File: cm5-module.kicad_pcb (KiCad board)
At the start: 4 copper layers, 100 x 100 mm, 205 parts, among them J1 DIN-41612-connector_090319679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, J10 MicroSD_5033981892, J11 JST_SH_1x4_BM04B-SRSS-TB-LF-SN, J2 CM5_1-100_3mm-stack, J3 CM5_101-200_3mm-stack, J4 JST_SH_1x3_BM03B-SRSS-TB-LF-SN, J5 Bus_M.2_1-2199230-6, J6 RJ45_HC612601A-M893-A, J7 USB-A_USB-303WSD-BRY, J8 HDMI-A_HDMI-19PIN-043, J9 USB-C_USB-310F-B-SU, Q1 SIS472DN-T1-GE3, Q2 SIS472DN-T1-GE3, Q3 AO3400A, Q4 SIS472DN-T1-GE3, SW1 SW_TL2243, U1 AP22615AWU-7, U10 AP22615AWU-7, U11 AP22615AWU-7, U12 LM74700QDBVRQ1, U13 STM32G431CBU6, U14 STM32G431CBU6, U15 TJA1044GTK_3Z, U16 TJA1044GTK_3Z, U2 AP22615AWU-7, U3 FT230XQ-R, U4 NTS0102DP, U5 CH334P, U6 LM74700QDBVRQ1, U7 SIC431AED-T1-GE3, U8 LM74700QDBVRQ1, U9 TPS564247DRLR, Y1 Oscillator_32.768kHz_OK2EL89C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, Y2 X322512MSB4SI

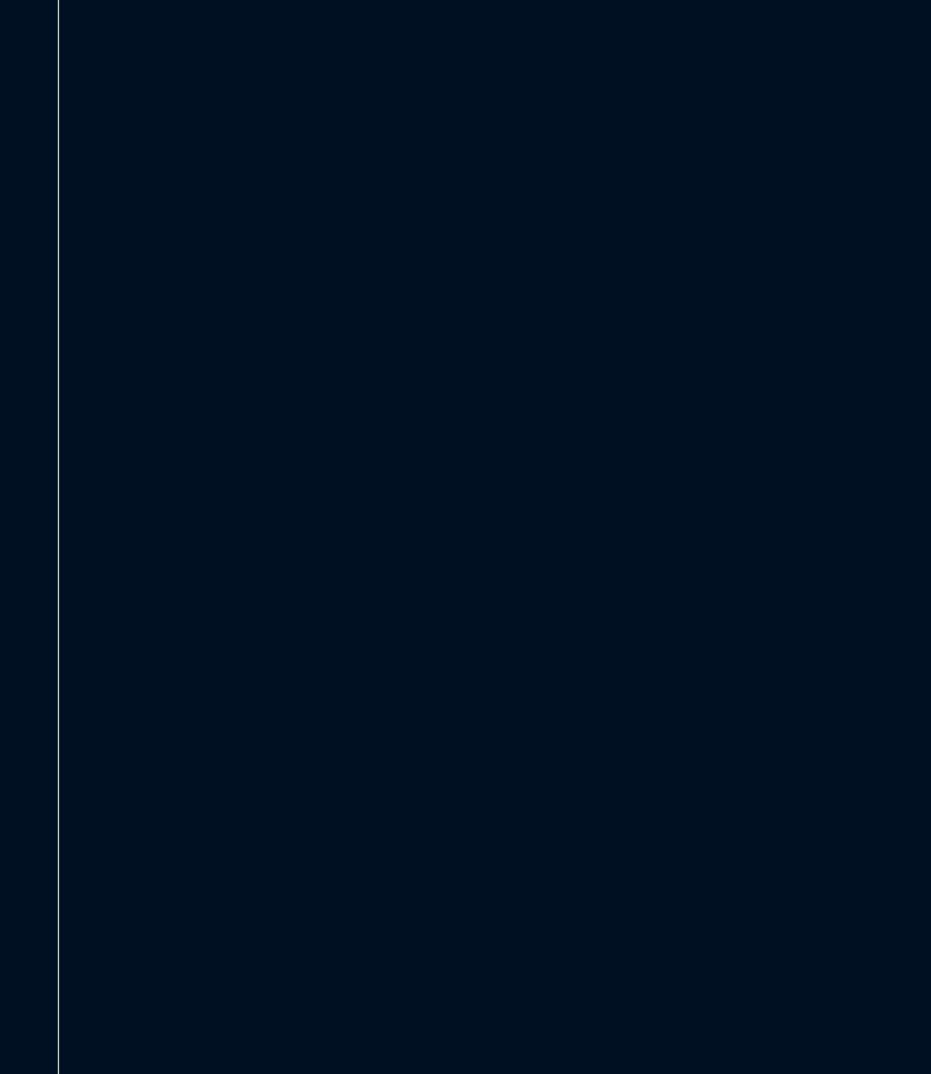
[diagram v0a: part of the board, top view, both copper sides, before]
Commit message: [#1] Add USB switch and 0R to USB hub data lines, minor schematic refactor
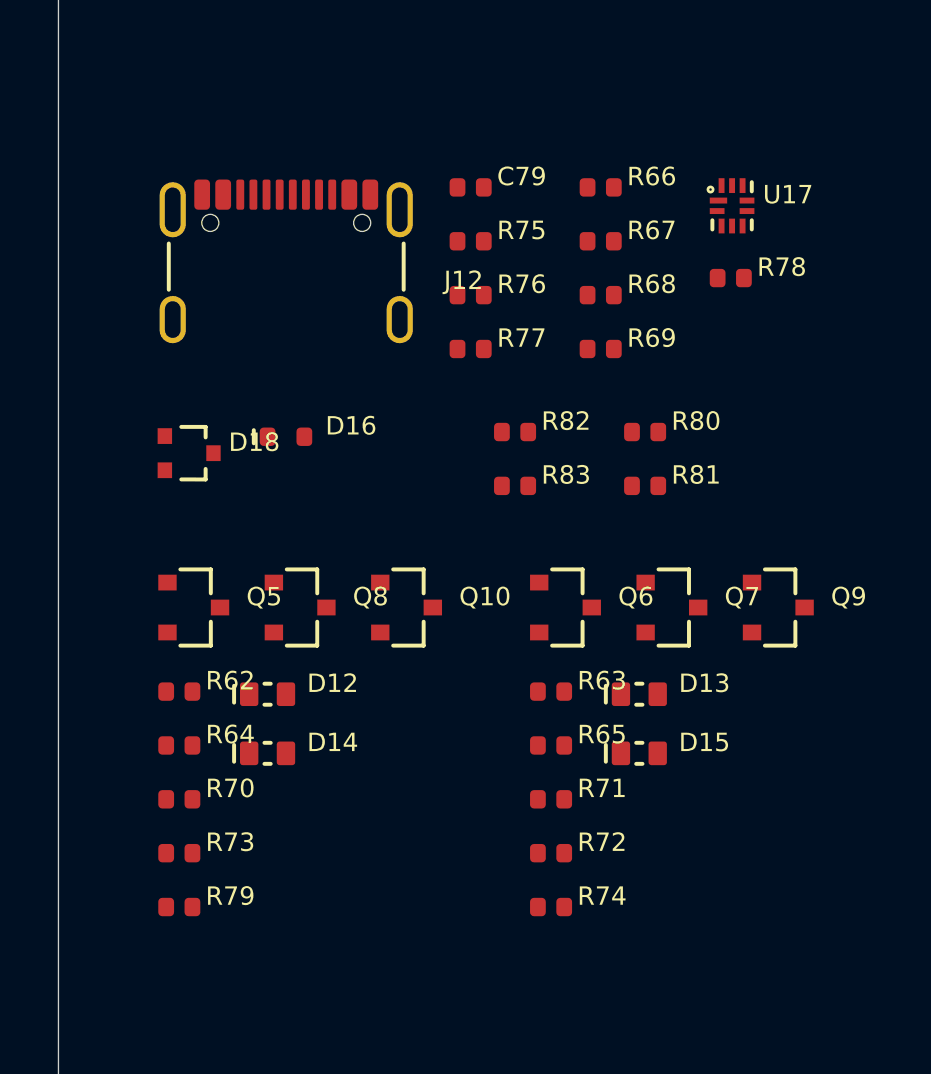
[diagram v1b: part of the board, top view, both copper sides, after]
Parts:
- added C79: C-100n-0402, DW-footprints:C_0402_1005Metric, F.Cu at (155.1, 67.2)
- added D12: LED-R-0603_KT-0603R, DW-footprints:LED_0603_1608Metric_R, F.Cu at (147.3, 86.5)
- added D13: LED-R-0603_KT-0603R, DW-footprints:LED_0603_1608Metric_R, F.Cu at (161.5, 86.5)
- added D14: LED-R-0603_KT-0603R, DW-footprints:LED_0603_1608Metric_R, F.Cu at (147.3, 88.8)
- added D15: LED-R-0603_KT-0603R, DW-footprints:LED_0603_1608Metric_R, F.Cu at (161.5, 88.8)
- added D16: PESD5Z5, DW-footprints:D_SOD-523, F.Cu at (148.0, 76.7)
- added D18: TPD2E2U06DCKR, DW-footprints:SOT-323, F.Cu at (144.3, 77.3)
- added J12: USB-C_USB-310F-B-SU, DW-footprints:USB-C-Receptacle_USB-310-B-SU, F.Cu at (148.0, 71.2)
- added Q10: AO3400A, DW-footprints:SOT-23-3, F.Cu at (152.6, 83.2)
- added Q5: AO3400A, DW-footprints:SOT-23-3, F.Cu at (144.5, 83.2)
- added Q6: AO3400A, DW-footprints:SOT-23-3, F.Cu at (158.7, 83.2)
- added Q7: AO3400A, DW-footprints:SOT-23-3, F.Cu at (162.7, 83.2)
- added Q8: AO3401A, DW-footprints:SOT-23-3, F.Cu at (148.6, 83.2)
- added Q9: AO3401A, DW-footprints:SOT-23-3, F.Cu at (166.8, 83.2)
- added R62: R-1k-0402, DW-footprints:R_0402_1005Metric, F.Cu at (144.0, 86.4)
- added R63: R-1k-0402, DW-footprints:R_0402_1005Metric, F.Cu at (158.1, 86.4)
- added R64: R-1k-0402, DW-footprints:R_0402_1005Metric, F.Cu at (144.0, 88.5)
- added R65: R-1k-0402, DW-footprints:R_0402_1005Metric, F.Cu at (158.1, 88.5)
- added R66: R-0R-0402, DW-footprints:R_0402_1005Metric, F.Cu at (160.0, 67.2)
- added R67: R-0R-0402, DW-footprints:R_0402_1005Metric, F.Cu at (160.0, 69.3)
- added R68: R-0R-0402, DW-footprints:R_0402_1005Metric, F.Cu at (160.0, 71.3)
- added R69: R-0R-0402, DW-footprints:R_0402_1005Metric, F.Cu at (160.0, 73.4)
- added R70: R-10k-0402, DW-footprints:R_0402_1005Metric, F.Cu at (144.0, 90.5)
- added R71: R-10k-0402, DW-footprints:R_0402_1005Metric, F.Cu at (158.1, 90.5)
- added R72: R-10k-0402, DW-footprints:R_0402_1005Metric, F.Cu at (158.1, 92.6)
- added R73: R-10k-0402, DW-footprints:R_0402_1005Metric, F.Cu at (144.0, 92.6)
- added R74: R-10k-0402, DW-footprints:R_0402_1005Metric, F.Cu at (158.1, 94.6)
- added R75: R-330r-0402, DW-footprints:R_0402_1005Metric, F.Cu at (155.1, 69.3)
- added R76: R-5k1-0402, DW-footprints:R_0402_1005Metric, F.Cu at (155.1, 71.3)
- added R77: R-5k1-0402, DW-footprints:R_0402_1005Metric, F.Cu at (155.1, 73.4)
- added R78: R-10k-0402, DW-footprints:R_0402_1005Metric, F.Cu at (165.0, 70.7)
- added R79: R-10k-0402, DW-footprints:R_0402_1005Metric, F.Cu at (144.0, 94.6)
- added R80: R-10k-0402, DW-footprints:R_0402_1005Metric, F.Cu at (161.7, 76.5)
- added R81: R-10k-0402, DW-footprints:R_0402_1005Metric, F.Cu at (161.7, 78.6)
- added R82: R-0R-0402, DW-footprints:R_0402_1005Metric, F.Cu at (156.8, 76.5)
- added R83: R-0R-0402, DW-footprints:R_0402_1005Metric, F.Cu at (156.8, 78.6)
- added U17: FSUSB42UMX, DW-footprints:UFQFN-10_1.4x1.8mm_P0.4mm, F.Cu at (165.0, 67.9)
- R27, R28, R29, R30, R31, R32, R33, R34: value R-220r-0402 -> R-0R-0402
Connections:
- net /2xUSB3.0/+VBUS renamed /USB/+VBUS
- net /2xUSB3.0/EN renamed /USB/EN
- net /2xUSB3.0/FLG renamed /USB/FLG
- net /2xUSB3.0/ISET renamed /USB/ISET
- net /2xUSB3.0/USB_SS_0.D+ renamed /CM5/USB_SS_0.D+
- net /2xUSB3.0/USB_SS_0.D- renamed /CM5/USB_SS_0.D-
- net /2xUSB3.0/USB_SS_0.RX+ renamed /CM5/USB_SS_0.RX+
- net /2xUSB3.0/USB_SS_0.RX- renamed /CM5/USB_SS_0.RX-
- net /2xUSB3.0/USB_SS_0.TX+ renamed /CM5/USB_SS_0.TX+
- net /2xUSB3.0/USB_SS_0.TX- renamed /CM5/USB_SS_0.TX-
- net /2xUSB3.0/USB_SS_1.D+ renamed /CM5/USB_SS_1.D+
- net /2xUSB3.0/USB_SS_1.D- renamed /CM5/USB_SS_1.D-
- net /2xUSB3.0/USB_SS_1.RX+ renamed /CM5/USB_SS_1.RX+
- net /2xUSB3.0/USB_SS_1.RX- renamed /CM5/USB_SS_1.RX-
- net /2xUSB3.0/USB_SS_1.TX+ renamed /CM5/USB_SS_1.TX+
- net /2xUSB3.0/USB_SS_1.TX- renamed /CM5/USB_SS_1.TX-
- net /2xUSB3.0/VBUS_EN renamed /CM5/VBUS_EN
- net /CAN to USB/RXD renamed /CAN to USB 1/RXD
- net /CAN to USB/TXD renamed /CAN to USB 1/TXD
- net /CAN to USB/~{RST} renamed /CAN to USB 1/~{RST}
- net /CAN to USB1/RXD renamed /CAN to USB 2/RXD
- net /CAN to USB1/TXD renamed /CAN to USB 2/TXD
- net /CAN to USB1/~{RST} renamed /CAN to USB 2/~{RST}
- net Net-(U15-VIO) renamed /CAN to USB 1/VIO
- net Net-(U16-VIO) renamed /CAN to USB 2/VIO
- J2 pad 28: unconnected-(J2-GPIO13-Pad28) -> Net-(J2-GPIO13)
- J2 pad 31: unconnected-(J2-GPIO12-Pad31) -> Net-(J2-GPIO12)
- J2 pad 38: unconnected-(J2-GPIO11-Pad38) -> Net-(J2-GPIO11)
- J2 pad 44: unconnected-(J2-GPIO10-Pad44) -> Net-(J2-GPIO10)
- R27 pad 1: /CAN to USB/USB.D+ -> /USB hub/USB_1_R.D+
- R27 pad 2: /USB hub/USB_1_R.D+ -> /CAN to USB 1/USB.D+
- R28 pad 1: /CAN to USB/USB.D- -> /USB hub/USB_1_R.D-
- R28 pad 2: /USB hub/USB_1_R.D- -> /CAN to USB 1/USB.D-
- R29 pad 1: /CAN to USB1/USB.D+ -> /USB hub/USB_2_R.D+
- R29 pad 2: /USB hub/USB_2_R.D+ -> /CAN to USB 2/USB.D+
- R30 pad 1: /CAN to USB1/USB.D- -> /USB hub/USB_2_R.D-
- R30 pad 2: /USB hub/USB_2_R.D- -> /CAN to USB 2/USB.D-
- R31 pad 1: /Backplane/BACKPLANE.D+ -> /USB hub/USB_3_R.D+
- R31 pad 2: /USB hub/USB_3_R.D+ -> /Backplane/BACKPLANE.D+
- R32 pad 1: /Backplane/BACKPLANE.D- -> /USB hub/USB_3_R.D-
- R32 pad 2: /USB hub/USB_3_R.D- -> /Backplane/BACKPLANE.D-
- R33 pad 1: /USB hub/USB_4.D+ -> /USB hub/USB_4_R.D+
- R33 pad 2: /USB hub/USB_4_R.D+ -> /USB hub/USB_4.D+
- R34 pad 1: /USB hub/USB_4.D- -> /USB hub/USB_4_R.D-
- R34 pad 2: /USB hub/USB_4_R.D- -> /USB hub/USB_4.D-
- TP1 pad 1: /~{PWR_OFF} -> /CM5/PMIC_EN
- U13 pad 33: /CAN to USB/USB.D- -> /CAN to USB 1/USB.D-
- U13 pad 34: /CAN to USB/USB.D+ -> /CAN to USB 1/USB.D+
- U13 pad 38: /CAN to USB/STAT_LED -> /CAN to USB 1/STAT_LED
- U13 pad 8: /CAN to USB/WORD_LED -> /CAN to USB 1/WORD_LED
- U14 pad 33: /CAN to USB1/USB.D- -> /CAN to USB 2/USB.D-
- U14 pad 34: /CAN to USB1/USB.D+ -> /CAN to USB 2/USB.D+
- U14 pad 38: /CAN to USB1/STAT_LED -> /CAN to USB 2/STAT_LED
- U14 pad 8: /CAN to USB1/WORD_LED -> /CAN to USB 2/WORD_LED
- U5 pad 11: /CM5/USB.D- -> /USB hub/USB_HUB.D-
- U5 pad 12: /CM5/USB.D+ -> /USB hub/USB_HUB.D+

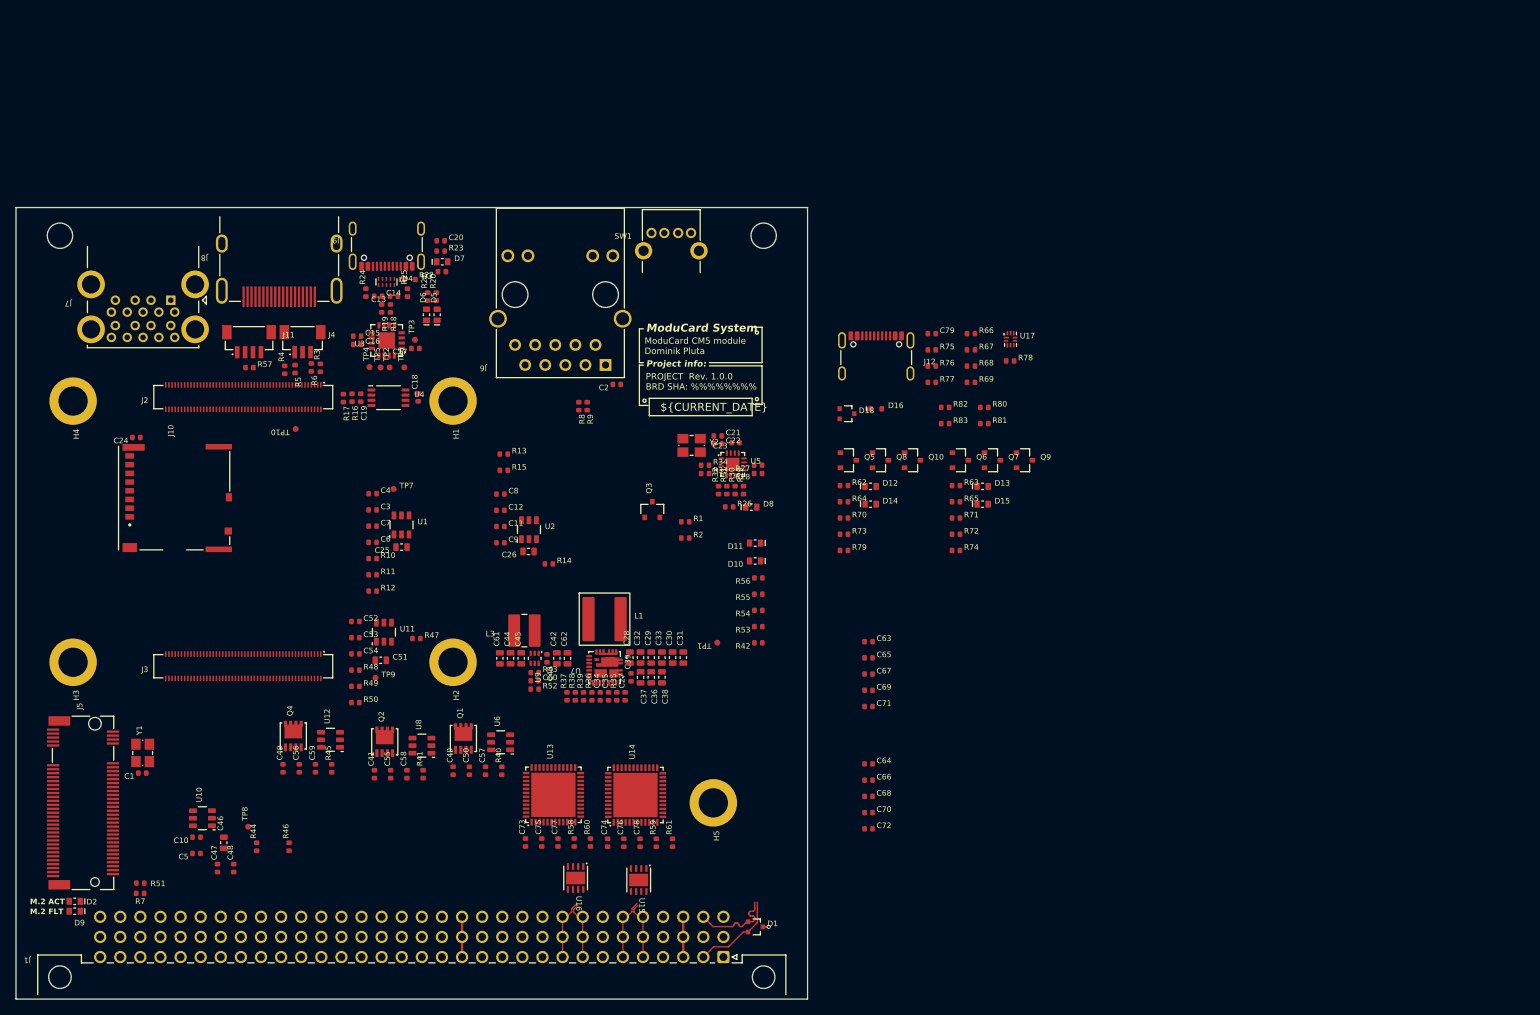
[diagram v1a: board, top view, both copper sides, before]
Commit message: [#3] Align PCB to grid, start placement of key components
Position the M.2 connector, try positioning of front panel connectors
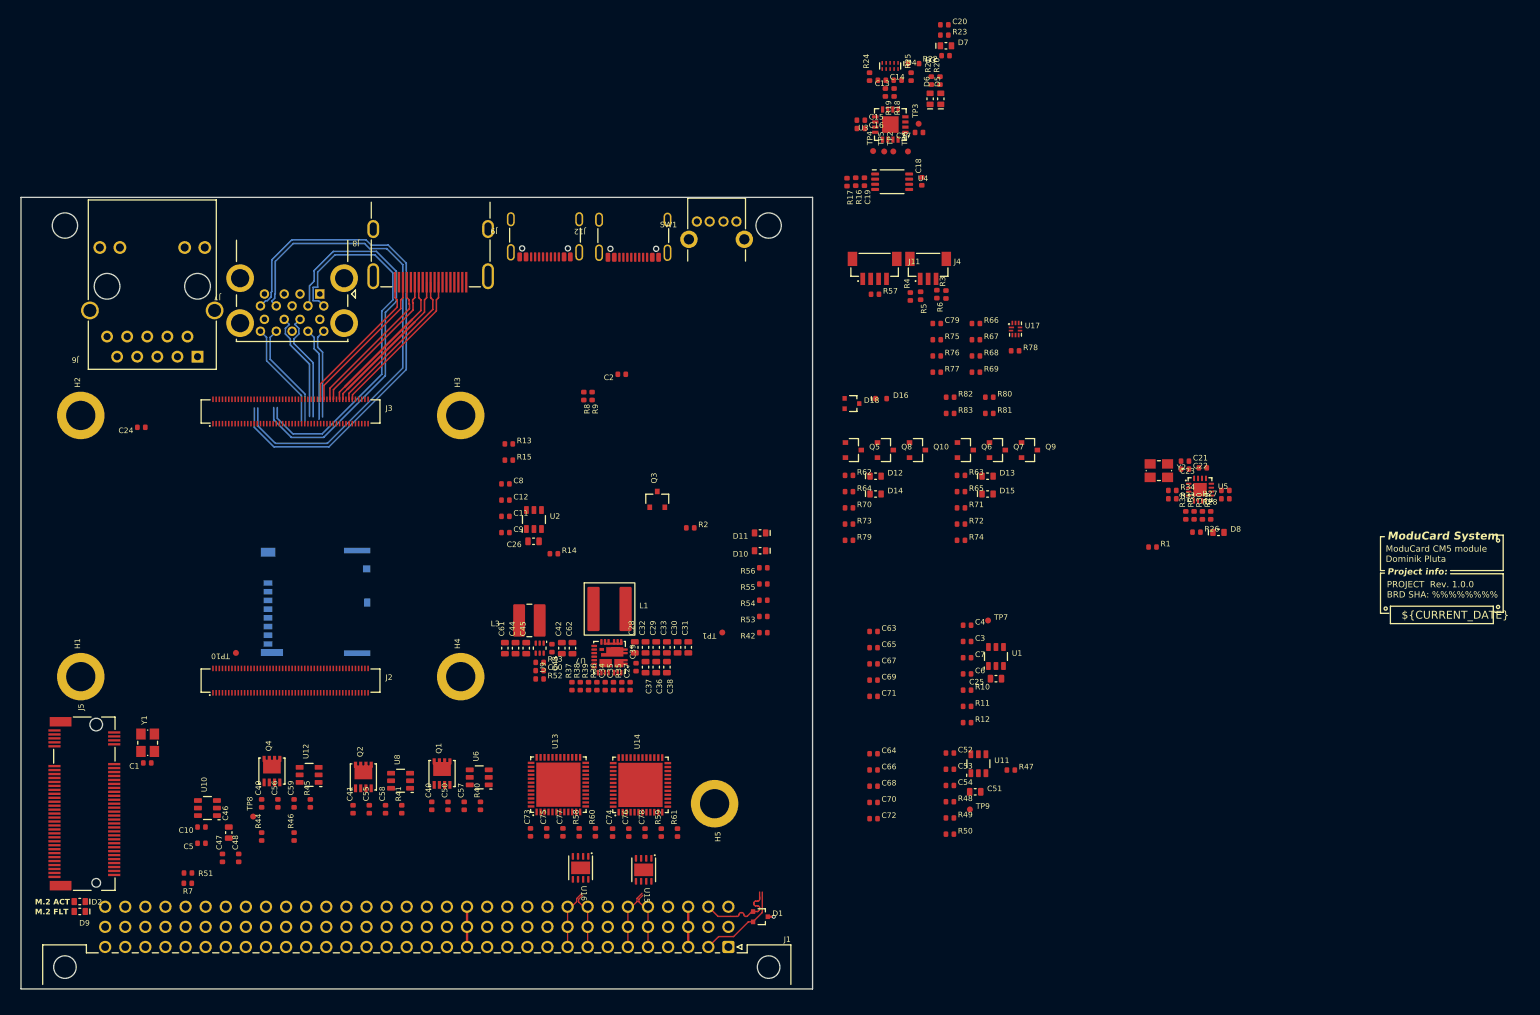
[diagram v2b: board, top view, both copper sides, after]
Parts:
- J10: moved to B.Cu
- moved J11 79.6 mm to (147.8, 58.5)
- moved J4 79.6 mm to (154.6, 58.5)
- moved R3 79.6 mm to (156.8, 62.3)
- moved R4 79.6 mm to (152.3, 62.5)
- moved R5 79.6 mm to (153.7, 62.4)
- moved R57 79.6 mm to (147.9, 62.2)
- moved R6 79.6 mm to (155.7, 62.2)
- moved C3 76.9 mm to (159.5, 106.1)
- moved C4 76.9 mm to (159.5, 104.1)
- moved C51 76.9 mm to (160.6, 125.1)
- moved C6 76.9 mm to (159.5, 110.2)
- moved C7 76.9 mm to (159.5, 108.2)
- moved R10 76.9 mm to (159.5, 112.3)
- moved R11 76.9 mm to (159.5, 114.3)
- moved R12 76.9 mm to (159.5, 116.4)
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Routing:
- net /CM5/USB_SS_0.RX-: track 0.00 -> 65.9 mm
- net /CM5/USB_SS_0.RX+: track 0.00 -> 62.7 mm
- net /CM5/USB_SS_0.TX-: track 0.00 -> 50.9 mm
- net /CM5/USB_SS_0.TX+: track 0.00 -> 49.0 mm
- net /CM5/HDMI_0.D0+: track 0.00 -> 43.4 mm
- net /CM5/HDMI_0.D0-: track 0.00 -> 43.4 mm
- net /CM5/HDMI_0.CLK+: track 0.00 -> 19.3 mm
- net /CM5/HDMI_0.CLK-: track 0.00 -> 19.3 mm
- net /CM5/HDMI_0.D1+: track 0.00 -> 19.1 mm
- net /CM5/HDMI_0.D1-: track 0.00 -> 19.1 mm
- net /CM5/HDMI_0.D2+: track 0.00 -> 18.9 mm
- net /CM5/HDMI_0.D2-: track 0.00 -> 18.9 mm
- net /CM5/USB_SS_1.D-: track 0.00 -> 14.1 mm
- net /CM5/USB_SS_1.D+: track 0.00 -> 14.0 mm
- net /CM5/USB_SS_1.RX-: track 0.00 -> 13.6 mm
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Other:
- outline, holes or cut-outs redrawn
